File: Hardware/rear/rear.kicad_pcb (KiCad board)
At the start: 4 copper layers, 56 x 46.5 mm, 25 parts, among them J101 Conn_02x10_Odd_Even, J102 USB_B, J103 ARJC07-111071A, J104 CRJ061-L1-TH, U101 AT24CS32-SSHM, U102 WE-TVS-82400102, U103 XRA1200

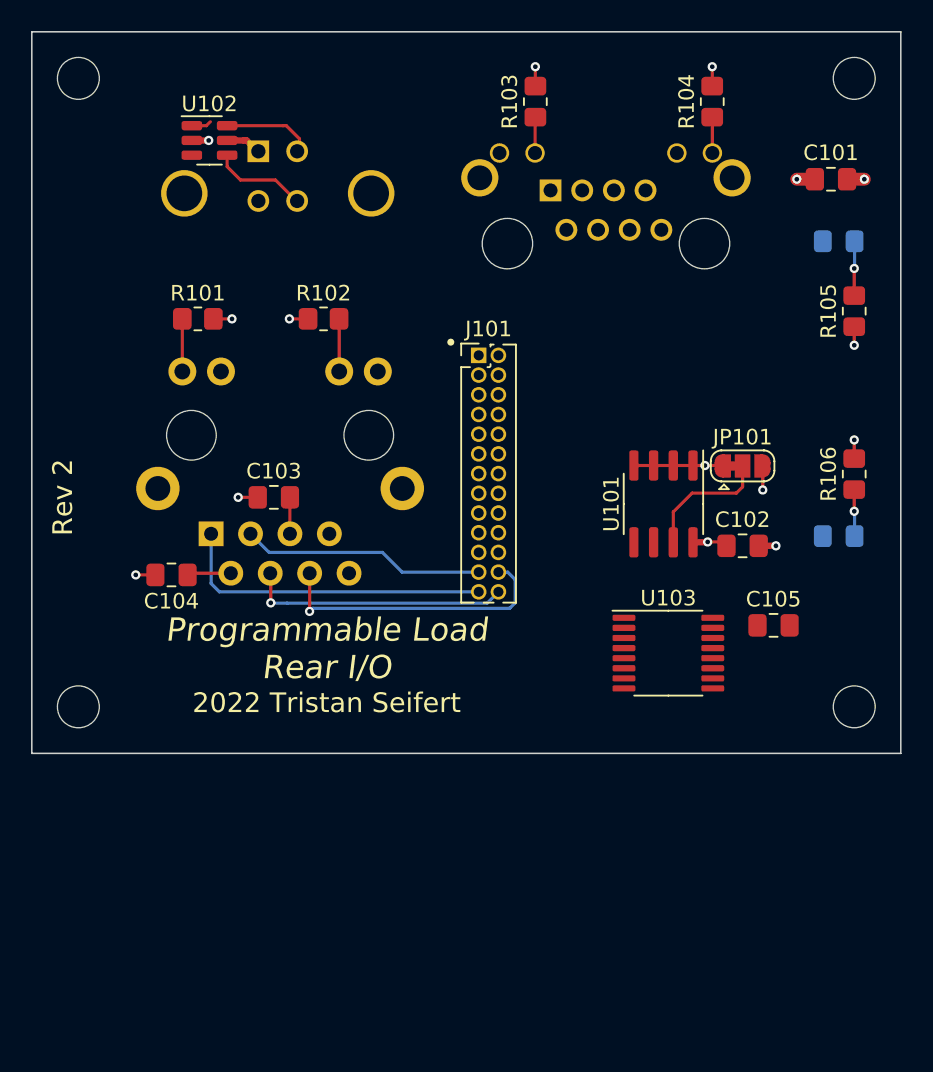
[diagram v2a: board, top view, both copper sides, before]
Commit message: Rear IO rework
- Mostly finished the rear IO board rework (adding the CAN filtering and
  switchable termination; trigger input pulse shaper; fuses for
  expansion +12V)

- Changed encoder type on front panel for a shorter type

- Created schematic models and footprints for Bournds DR311 chokes;
  Mill-Max 2108 solder turrets
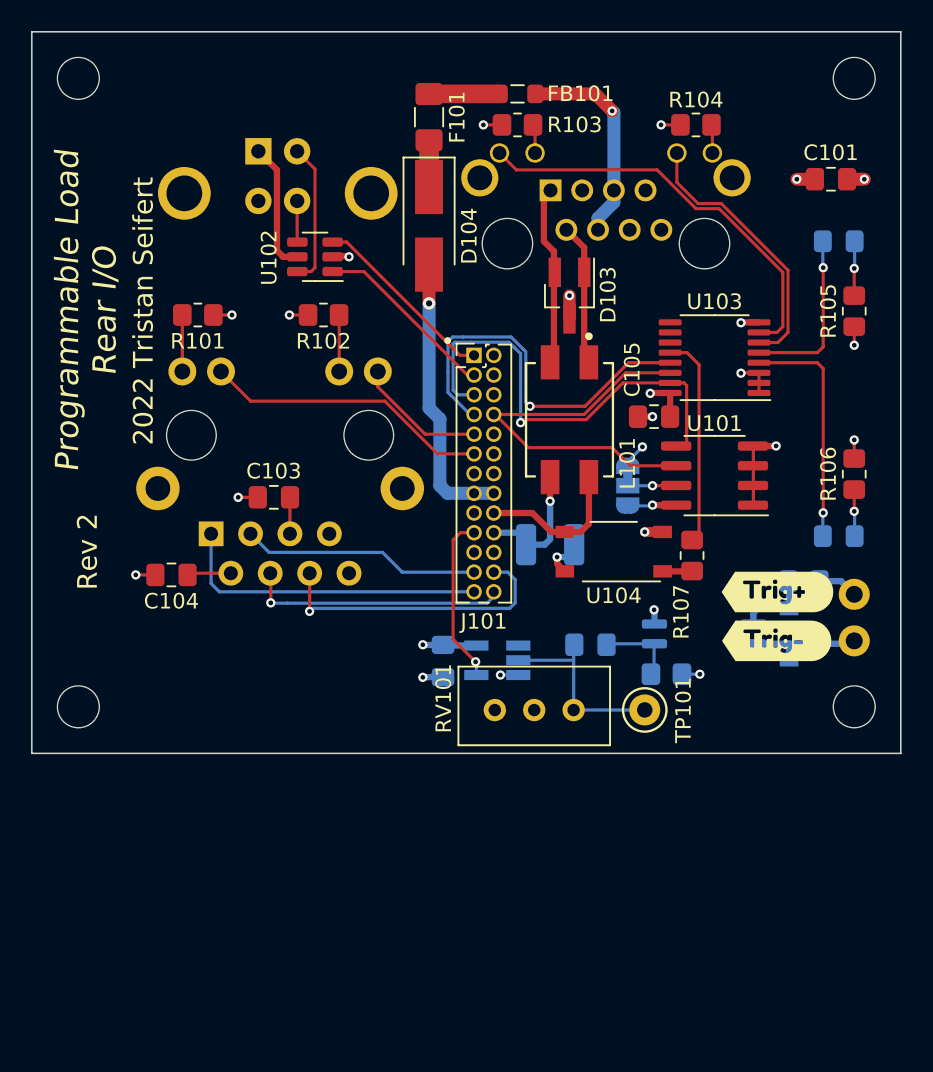
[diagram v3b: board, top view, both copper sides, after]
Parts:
- added C106: 100nF, Capacitor_SMD:C_0805_2012Metric_Pad1.18x1.45mm_HandSolder, B.Cu at (46.5, 60.5)
- added D103: ESDONCAN1, Package_TO_SOT_SMD:SOT-23_Handsoldering, F.Cu at (54.6, 37.0)
- added D104: Panjit SS14, Diode_SMD:D_SMA_Handsoldering, F.Cu at (45.6, 32.5)
- added D105: 1N4148W, Diode_SMD:D_SOD-123, B.Cu at (68.8, 58.8)
- added F101: 500mA, Fuse:Fuse_1206_3216Metric_Pad1.42x1.75mm_HandSolder, F.Cu at (45.6, 25.5)
- added FB101: FerriteBead_Small, Inductor_SMD:L_0805_2012Metric_Pad1.05x1.20mm_HandSolder, F.Cu at (51.3, 24.0)
- added J105: Conn_01x01, programmable-load:MillMax-2108-2, F.Cu at (73.0, 56.2)
- added J106: Conn_01x01, programmable-load:MillMax-2108-2, F.Cu at (73.0, 59.2)
- added L101: DR331-513BE, programmable-load:Bourns-DR331-0-0-MFG, F.Cu at (54.6, 45.0)
- added R107: 1k, Resistor_SMD:R_0805_2012Metric_Pad1.20x1.40mm_HandSolder, F.Cu at (62.5, 53.8)
- added R108: 100R, Resistor_SMD:R_1210_3225Metric_Pad1.30x2.65mm_HandSolder, B.Cu at (53.4, 53.0)
- added R109: 200R, Resistor_SMD:R_0805_2012Metric_Pad1.20x1.40mm_HandSolder, B.Cu at (69.8, 55.4)
- added R110: 47k, Resistor_SMD:R_0805_2012Metric_Pad1.20x1.40mm_HandSolder, B.Cu at (60.9, 61.4)
- added RV101: 500k, programmable-load:Potentiometer_Nidec_Copal_CT94EW, F.Cu at (57.4, 66.0)
- added TP101: Trigger, TestPoint:TestPoint_Keystone_5000-5004_Miniature, F.Cu at (59.5, 63.7)
- added U104: TLP170A, Package_SO:MFSOP6-4_4.4x3.6mm_P1.27mm, F.Cu at (57.5, 53.5)
- added U105: FODM217B, Package_SO:SOP-4_4.4x2.6mm_P1.27mm, B.Cu at (63.3, 58.8)
- added U106: 74LVC1G17, Package_TO_SOT_SMD:SOT-23-5_HandSoldering, B.Cu at (50.0, 60.5)
- added kibuzzard-62664110: G***, kibuzzard-62664110, F.Cu at (68.0, 59.2)
- added kibuzzard-62664123: G***, kibuzzard-62664123, F.Cu at (68.0, 56.1)
- C102: value 100nF -> 1µF; moved to B.Cu
- JP101: moved to B.Cu
- moved U103 19.3 mm to (64.0, 41.0), turned to 180 degrees
- moved C105 15.5 mm to (60.1, 44.8), turned to 180 degrees
- moved C102 11.7 mm to (56.0, 59.5)
- moved U102 10.1 mm to (38.2, 34.5), turned to 180 degrees
- moved JP101 7.51 mm to (58.4, 49.2), turned to -90 degrees
- moved U101 3.77 mm to (64.0, 48.6), turned to 180 degrees
- moved R103 1.89 mm to (51.3, 26.0), turned to 180 degrees
- moved R104 1.83 mm to (62.8, 26.0), turned to 180 degrees
- moved J101 0.30 mm to (48.5, 40.9)
- moved R101 0.25 mm to (30.7, 38.2)
- moved R102 0.25 mm to (38.8, 38.2)
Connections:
- C102 pad 1: +3V3 -> Net-(C102-Pad1)
- C102 pad 2: GND -> Net-(U105-Pad3)
- D101 pad 1: unconnected-(D101-Pad1) -> /~{LED_VSENSE}
- D102 pad 1: unconnected-(D102-Pad1) -> /~{LED_TRIGGER}
- J101 pad 15: GND -> +12V
- J101 pad 16: GND -> +12V
- J101 pad 17: unconnected-(J101-Pad17) -> GND
- J101 pad 18: /CAN- -> /CANL
- J101 pad 19: unconnected-(J101-Pad19) -> /TRIGGER
- J101 pad 20: /CAN+ -> /CANH
- J104 pad 1: unconnected-(J104-Pad1) -> Net-(D103-Pad2)
- J104 pad 11: unconnected-(J104-Pad11) -> /~{EXT_LED1}
- J104 pad 2: unconnected-(J104-Pad2) -> Net-(D103-Pad1)
- J104 pad 4: unconnected-(J104-Pad4) -> Net-(FB101-Pad1)
- J104 pad 5: unconnected-(J104-Pad5) -> Net-(FB101-Pad1)
- J104 pad 7: unconnected-(J104-Pad7) -> GND
- J104 pad 8: unconnected-(J104-Pad8) -> GND
- J104 pad 9: unconnected-(J104-Pad9) -> /~{EXT_LED0}
- J104 pad S2: unconnected-(J104-PadS1) -> unconnected-(J104-PadS2)
- U103 pad 12: unconnected-(U103-Pad12) -> /TERM_EN
- U103 pad 13: unconnected-(U103-Pad13) -> /~{IRQ}
- U103 pad 4: unconnected-(U103-Pad4) -> /~{LED_TRIGGER}
- U103 pad 5: unconnected-(U103-Pad5) -> /~{LED_VSENSE}
- U103 pad 6: unconnected-(U103-Pad6) -> /~{EXT_LED1}
- U103 pad 7: unconnected-(U103-Pad7) -> /~{EXT_LED0}
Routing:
- net /SDA: track 0.00 -> 29.1 mm, vias 0 -> 1
- net /~{EXT_LED0}: track 0.00 -> 26.6 mm
- net /SCL: track 0.00 -> 25.6 mm
- net /~{IRQ}: track 0.00 -> 24.9 mm, vias 0 -> 1
- net /ETH_LED0: track 0.00 -> 18.5 mm
- net +12V: track 0.00 -> 18.2 mm, vias 0 -> 1
- net /~{EXT_LED1}: track 0.00 -> 17.5 mm
- net /~{LED_TRIGGER}: track 0.00 -> 15.1 mm, vias 0 -> 1
- net /TERM_EN: track 0.00 -> 13.7 mm
- net Net-(FB101-Pad1): track 0.00 -> 13.5 mm, vias 0 -> 1
- net /USB_D+: track 0.00 -> 12.4 mm
- net Net-(C102-Pad1): track 0.00 -> 12.4 mm
- net Net-(D103-Pad2): track 0.00 -> 12.2 mm
- net /~{LED_VSENSE}: track 0.00 -> 11.1 mm, vias 0 -> 1
- net /USB_D-: track 1.30 -> 12.2 mm
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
